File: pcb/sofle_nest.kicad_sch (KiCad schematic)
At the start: 110 parts, among them J1 MJ-4PP-9, J2 Pheonix-1332645, J3 Conn_01x04, J4 FFC2B35-12-G_REVA2, SW1 SW_PUSH, SW10 SW_PUSH, SW11 SW_PUSH, SW12 SW_PUSH, SW13 SW_PUSH, SW14 SW_PUSH, SW15 SW_PUSH, SW16 SW_PUSH, SW17 SW_PUSH, SW18 SW_PUSH, SW19 SW_PUSH, SW2 SW_PUSH, SW20 SW_PUSH, SW21 SW_PUSH, SW22 SW_PUSH, SW23 SW_PUSH, SW24 SW_PUSH, SW25 Rotary_Encoder_Switch-Device, SW26 SW_PUSH, SW27 SW_PUSH, SW28 SW_PUSH, SW29 SW_PUSH, SW3 SW_PUSH, SW30 SW_PUSH, SW4 SW_PUSH, SW5 SW_PUSH, SW6 SW_PUSH, SW7 SW_PUSH, SW8 SW_PUSH, SW9 SW_PUSH, U2 kb2040

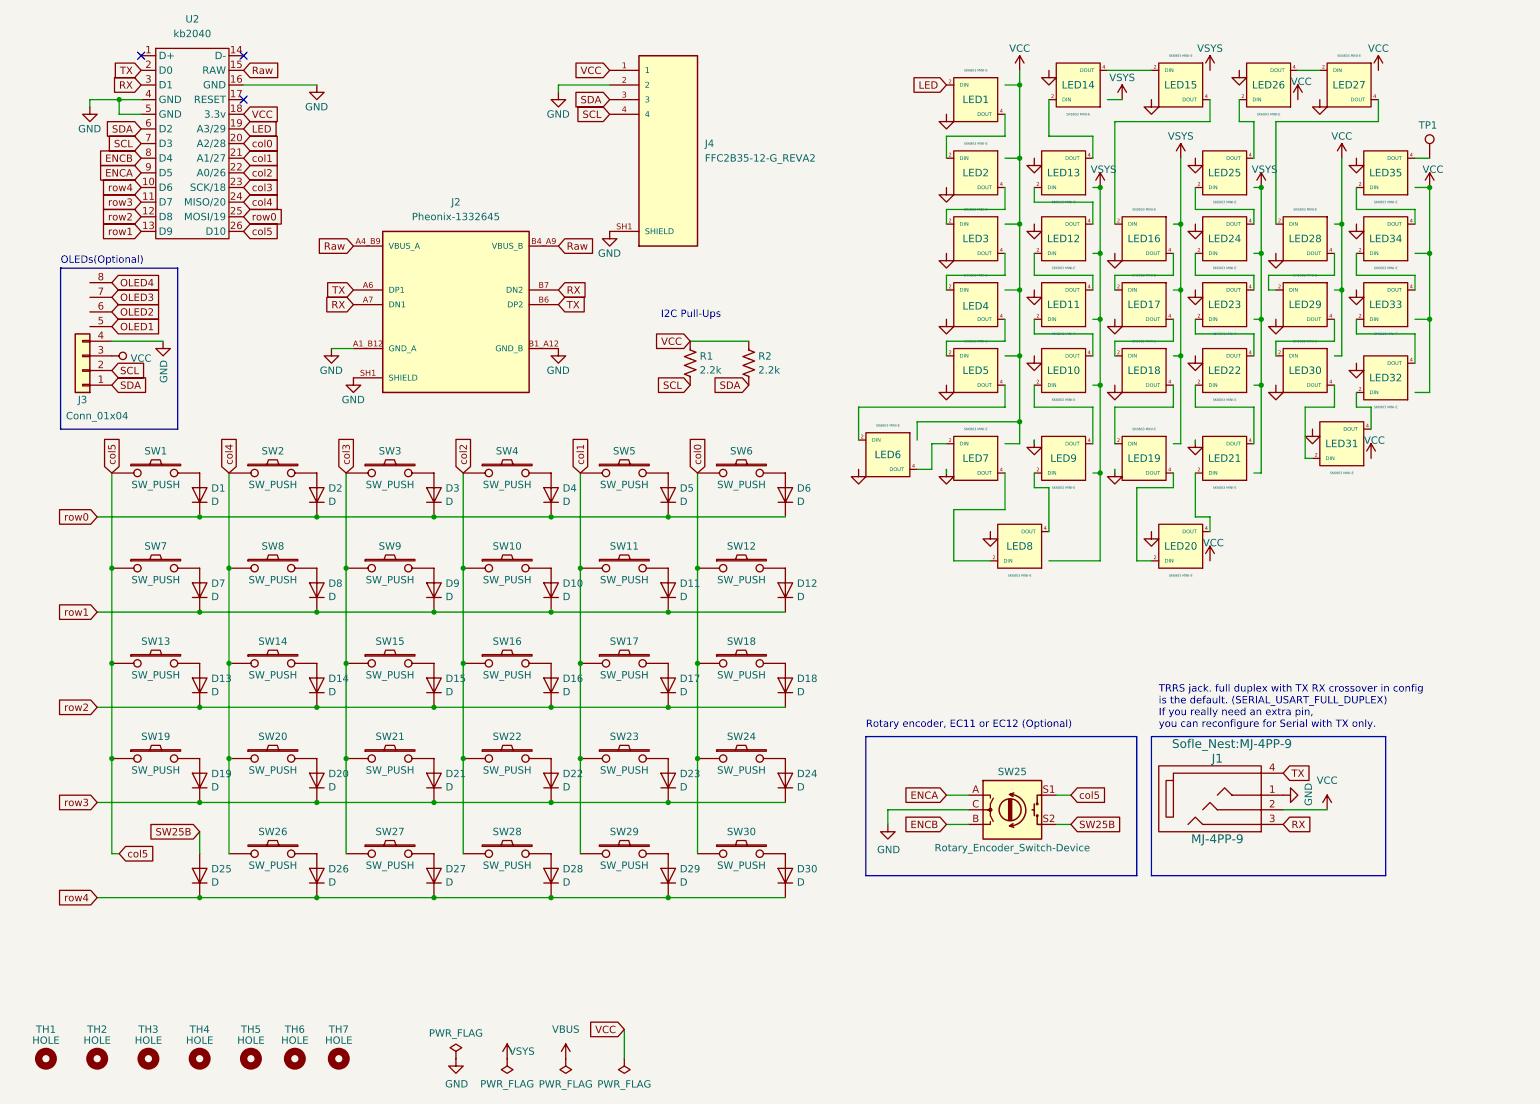
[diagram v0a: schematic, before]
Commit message: Re-route underglow leds to put the top ones in series
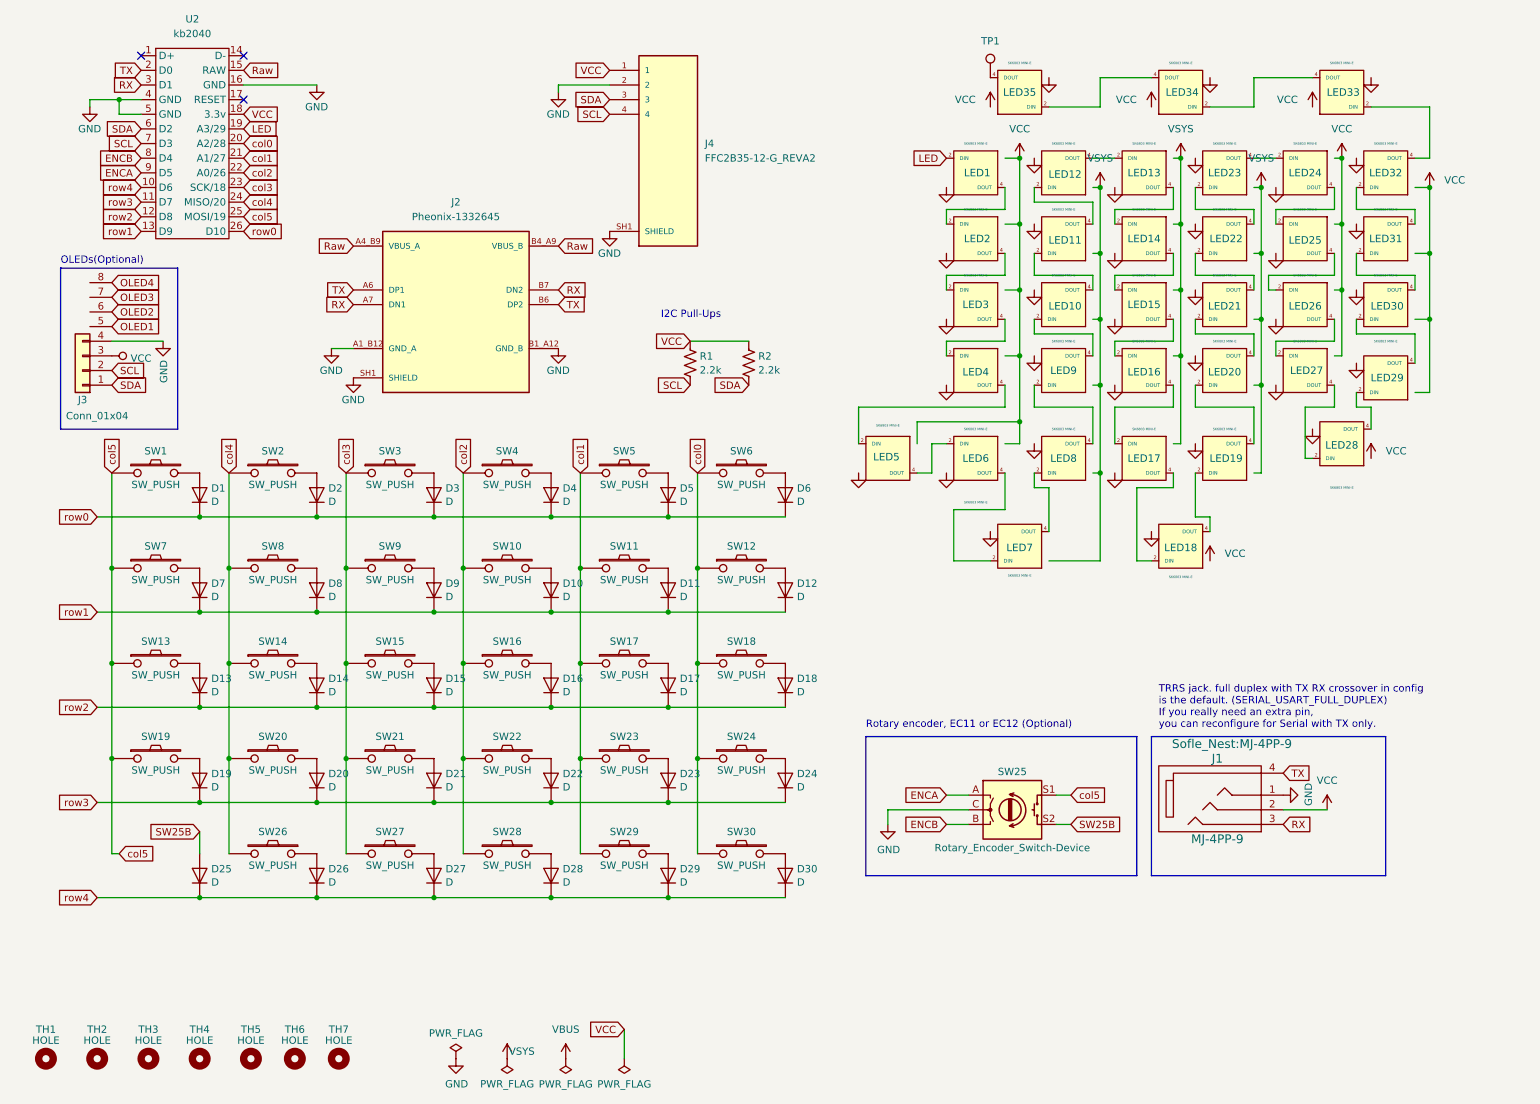
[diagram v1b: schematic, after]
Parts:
- LED1, LED20, LED31, LED8: footprint Sofle_Nest:DropLight_SK6803_MINI-E_v3.5.5 -> Sofle_Nest:SK6803_MINI-E_v3.5.5; symbol Sofle_Nest:DropLight_SK6803MINIE_V2 -> Sofle_Nest:SK6803MINIE_V2
- LED15, LED27: footprint Sofle_Nest:DropLight_SK6803_MINI-E_v3.5.5 -> Sofle_Nest:SK6803_MINI-E_v3.5.5
- LED18, LED28, LED33, LED34, LED35, LED7: footprint Sofle_Nest:SK6803_MINI-E_v3.5.5 -> Sofle_Nest:SK6803_MINI-E_v3.5.5_Underglow; symbol Sofle_Nest:SK6803MINIE_V2 -> Sofle_Nest:SK6803MINIE_V2_Underglow
- LED26: symbol Sofle_Nest:DropLight_SK6803MINIE_V2 -> Sofle_Nest:SK6803MINIE_V2
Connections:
- net col5: now also U2.25 (MOSI/19); no longer U2.26 (D10)
- net row0: now also U2.26 (D10); no longer U2.25 (MOSI/19)
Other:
- moved on the sheet: LED1, LED10, LED11, LED12, LED13, LED14, LED15, LED16, LED17, LED18, LED19, LED2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

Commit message: Update schematic to pass electrical check rules and rewrite LEDs row-wise
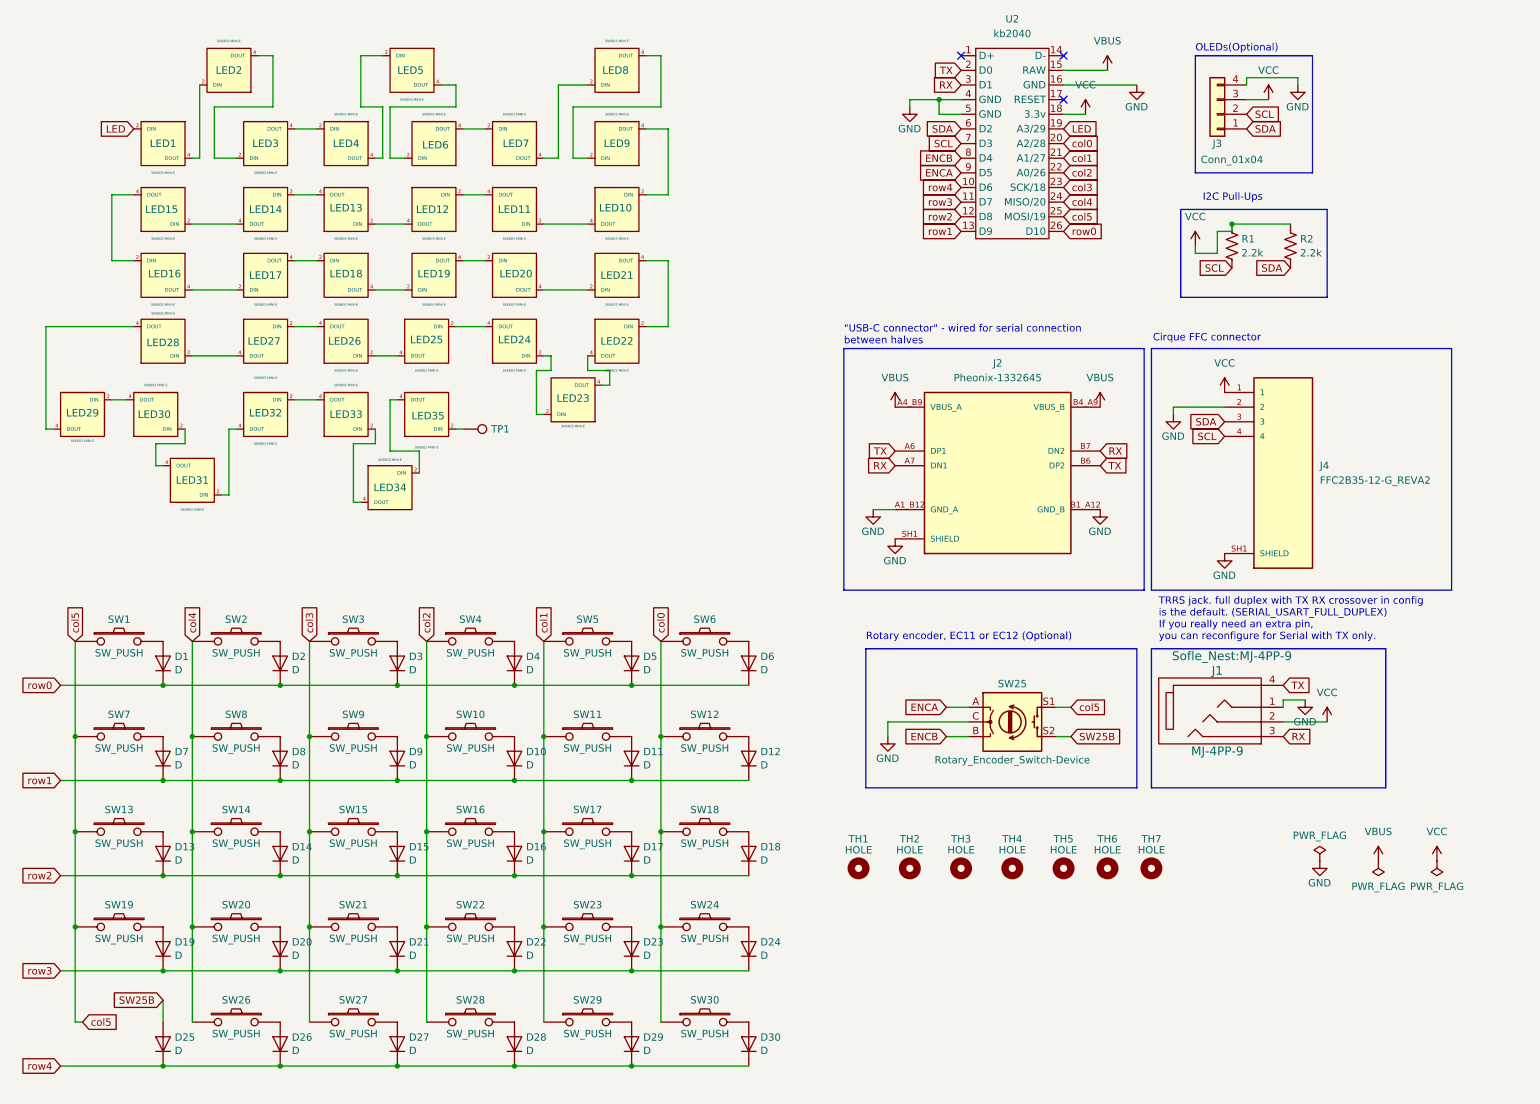
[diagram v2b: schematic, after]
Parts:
- J1: symbol Sofle_Pico:MJ-4PP-9 -> Sofle_Nest:MJ-4PP-9
- LED23: renamed from LED4; footprint Sofle_Nest:SK6803_MINI-E_v3.5.5 -> Sofle_Nest:SK6803_MINI-E_v3.5.5_Underglow; symbol Sofle_Nest:SK6803MINIE_V2 -> Sofle_Nest:SK6803MINIE_V2_Underglow
- LED28: renamed from LED18; footprint Sofle_Nest:SK6803_MINI-E_v3.5.5_Underglow -> Sofle_Nest:SK6803_MINI-E_v3.5.5; symbol Sofle_Nest:SK6803MINIE_V2_Underglow -> Sofle_Nest:SK6803MINIE_V2
- LED29: renamed from LED28; footprint Sofle_Nest:SK6803_MINI-E_v3.5.5_Underglow -> Sofle_Nest:SK6803_MINI-E_v3.5.5; symbol Sofle_Nest:SK6803MINIE_V2_Underglow -> Sofle_Nest:SK6803MINIE_V2
- LED31: renamed from LED17; footprint Sofle_Nest:SK6803_MINI-E_v3.5.5 -> Sofle_Nest:SK6803_MINI-E_v3.5.5_Underglow; symbol Sofle_Nest:SK6803MINIE_V2 -> Sofle_Nest:SK6803MINIE_V2_Underglow
- LED32: renamed from LED7; footprint Sofle_Nest:SK6803_MINI-E_v3.5.5_Underglow -> Sofle_Nest:SK6803_MINI-E_v3.5.5; symbol Sofle_Nest:SK6803MINIE_V2_Underglow -> Sofle_Nest:SK6803MINIE_V2
- LED34: renamed from LED6; footprint Sofle_Nest:SK6803_MINI-E_v3.5.5 -> Sofle_Nest:SK6803_MINI-E_v3.5.5_Underglow; symbol Sofle_Nest:SK6803MINIE_V2 -> Sofle_Nest:SK6803MINIE_V2_Underglow
- SW25: symbol Sofle_Pico:Rotary_Encoder_Switch-Device -> Sofle_Nest:Rotary_Encoder_Switch-Device
- renumbered LED23 to LED1, LED11 to LED10, LED14 to LED11, LED22 to LED12, LED25 to LED13, LED31 to LED14, LED2 to LED15, LED10 to LED16, LED15 to LED17, LED21 to LED18, LED26 to LED19, LED35 to LED2, LED30 to LED20, LED3 to LED21, LED9 to LED22, LED16 to LED24, LED20 to LED25, LED27 to LED26, LED29 to LED27, LED24 to LED3, LED19 to LED30, LED8 to LED33, LED5 to LED35, LED13 to LED4, LED34 to LED5, LED12 to LED6, LED1 to LED7, LED33 to LED8, LED32 to LED9
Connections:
- net Raw is gone; now on net VBUS: J2.A4_B9 (VBUS_A), J2.B4_A9 (VBUS_B), U2.15 (RAW)
- net LED: now also LED1.2 (DIN); no longer LED7.2 (DIN)
- net at LED22.2 (DIN): now also LED21.4 (DOUT); no longer LED33.4 (DOUT)
- net at LED22.4 (DOUT): now also LED23.4 (DOUT); no longer LED16.2 (DIN)
- net at LED14.2 (DIN): now also LED13.4 (DOUT); no longer LED20.4 (DOUT)
- net at LED14.4 (DOUT): now also LED15.2 (DIN); no longer LED9.2 (DIN)
- net at LED30.2 (DIN): now also LED31.4 (DOUT); no longer LED28.4 (DOUT)
- net at LED30.4 (DOUT): now also LED29.2 (DIN); no longer LED25.2 (DIN)
- net at LED21.2 (DIN): now also LED20.4 (DOUT); no longer LED15.4 (DOUT)
- net at LED23.2 (DIN): now also LED24.2 (DIN); no longer LED21.4 (DOUT)
- net at LED20.2 (DIN): now also LED19.4 (DOUT); no longer LED27.4 (DOUT)
- net at LED5.2 (DIN): now also LED4.4 (DOUT); no longer LED8.4 (DOUT)
- net at LED5.4 (DOUT): now also LED6.2 (DIN); no longer LED2.2 (DIN)
- net at LED31.2 (DIN): now also LED32.4 (DOUT); no longer LED24.4 (DOUT)
- net at LED28.2 (DIN): now also LED27.4 (DOUT); no longer LED31.4 (DOUT)
- net at LED4.2 (DIN): now also LED3.4 (DOUT); no longer LED6.4 (DOUT)
- net at LED11.2 (DIN): now also LED10.4 (DOUT); no longer LED4.4 (DOUT)
- net at LED9.4 (DOUT): now also LED10.2 (DIN); no longer LED8.2 (DIN)
- net at LED3.2 (DIN): now also LED2.4 (DOUT); no longer LED1.4 (DOUT)
- net at LED13.2 (DIN): now also LED12.4 (DOUT); no longer LED3.4 (DOUT)
- net at LED27.2 (DIN): now also LED26.4 (DOUT); no longer LED29.4 (DOUT)
- net at LED26.2 (DIN): now also LED25.4 (DOUT); no longer LED19.4 (DOUT)
- net at LED19.2 (DIN): now also LED18.4 (DOUT); no longer LED13.4 (DOUT)
- net at LED18.2 (DIN): now also LED17.4 (DOUT); no longer LED25.4 (DOUT)
- net at LED12.2 (DIN): now also LED11.4 (DOUT); no longer LED18.4 (DOUT)
- net at TP1.1: now also LED35.2 (DIN); no longer LED2.4 (DOUT)
- net at LED16.4 (DOUT): now also LED17.2 (DIN); no longer LED10.2 (DIN)
- net at LED33.2 (DIN): now also LED34.4 (DOUT); no longer LED32.4 (DOUT)
- net at LED7.4 (DOUT): now also LED8.2 (DIN); no longer LED15.2 (DIN)
- net at LED32.2 (DIN): now also LED33.4 (DOUT); no longer LED34.4 (DOUT)
- net OLED1: no longer names the net of J3.5 (Pin_1)
- net OLED2: no longer names the net of J3.6 (Pin_2)
- net OLED3: no longer names the net of J3.7 (Pin_3)
- net OLED4: no longer names the net of J3.8 (Pin_4)
- new net: LED8.4 (DOUT), LED9.2 (DIN)
- new net: LED28.4 (DOUT), LED29.4 (DOUT)
- new net: LED1.4 (DOUT), LED2.2 (DIN)
- new net: LED6.4 (DOUT), LED7.2 (DIN)
- new net: LED15.4 (DOUT), LED16.2 (DIN)
- new net: LED24.4 (DOUT), LED25.2 (DIN)
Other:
- note added: ""USB-C connector" - wired for serial connection between halves"
- note added: "Cirque FFC connector"
- moved on the sheet: D1, D10, D11, D12, D13, D14, D15, D16, D17, D18, D19, D2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

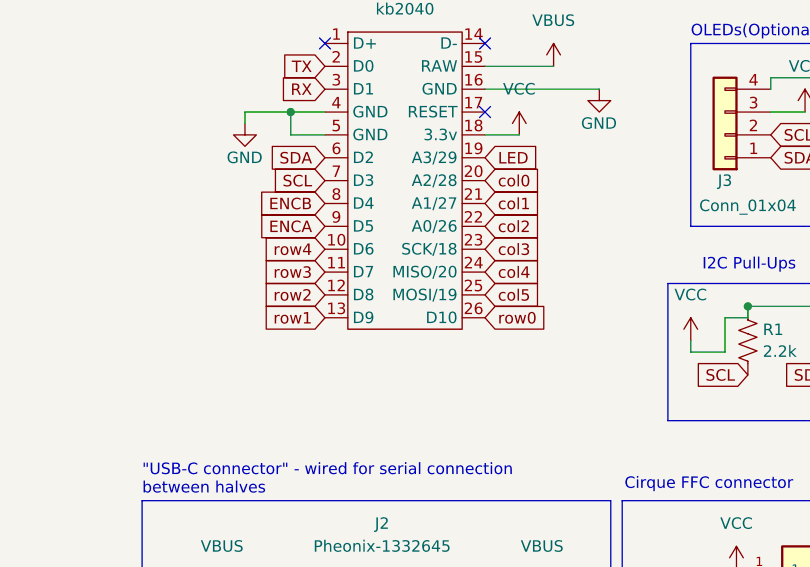
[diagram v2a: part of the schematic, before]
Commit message: Rewire rows and columns
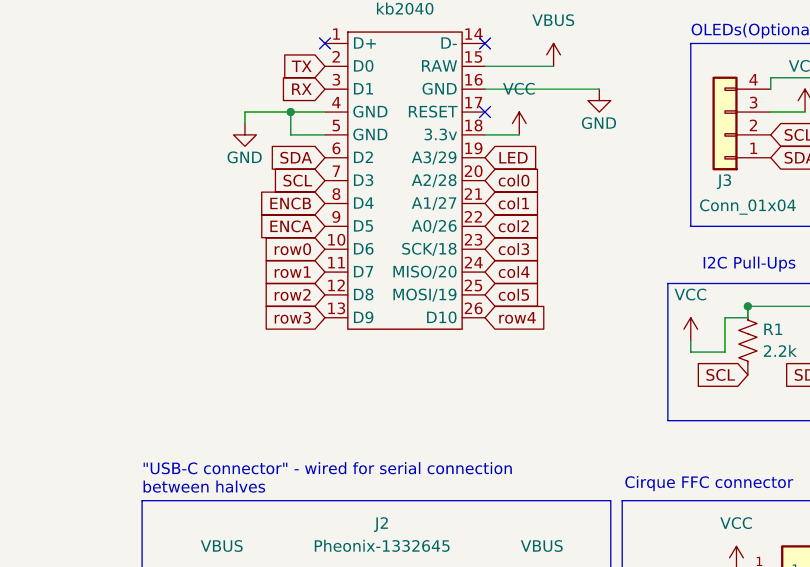
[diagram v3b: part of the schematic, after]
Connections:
- net row0: now also U2.10 (D6); no longer U2.26 (D10)
- net row1: now also U2.11 (D7); no longer U2.13 (D9)
- net row3: now also U2.13 (D9); no longer U2.11 (D7)
- net row4: now also U2.26 (D10); no longer U2.10 (D6)
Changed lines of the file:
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@@
-		)
-	)
-	(global_label "row0"
-		(shape input)
-		(at 195.58 53.34 0)
-		(effects
-			(font
-				(size 1.27 1.27)
-			)
-			(justify left)
-		)
-		(property "Intersheetrefs" "${INTERSHEET_REFS}"
-			(at 195.58 53.34 0)
-			(effects
-				(font
-					(size 1.27 1.27)
-				)
-				(hide yes)
-			)
 		)
 	)
@@
 		)
 	)
+	(global_label "row3"
+		(shape input)
+		(at 177.8 53.34 180)
+		(effects
+			(font
+				(size 1.27 1.27)
+			)
+			(justify right)
+		)
+		(property "Intersheetrefs" "${INTERSHEET_REFS}"
+			(at 177.8 53.34 0)
+			(effects
+				(font
+					(size 1.27 1.27)
+				)
+				(hide yes)
+			)
+		)
+	)
 	(global_label "LED"
 		(shape input)
@@
 		)
 	)
+	(global_label "row4"
+		(shape input)
+		(at 195.58 53.34 0)
+		(effects
+			(font
+				(size 1.27 1.27)
+			)
+			(justify left)
+		)
+		(property "Intersheetrefs" "${INTERSHEET_REFS}"
+			(at 195.58 53.34 0)
+			(effects
+				(font
+					(size 1.27 1.27)
+				)
+				(hide yes)
+			)
+		)
+	)
+	(global_label "row1"
+		(shape input)
+		(at 177.8 48.26 180)
+		(effects
+			(font
+				(size 1.27 1.27)
+			)
+			(justify right)
+		)
+		(property "Intersheetrefs" "${INTERSHEET_REFS}"
+			(at 177.8 48.26 0)
+			(effects
+				(font
+					(size 1.27 1.27)
+				)
+				(hide yes)
+			)
+		)
+	)
 	(global_label "TX"
 		(shape input)
@@
 		)
 	)
-	(global_label "row4"
+	(global_label "col3"
+		(shape input)
+		(at 64.77 124.46 90)
+		(effects
+			(font
+				(size 1.27 1.27)
+			)
+			(justify left)
+		)
+		(property "Intersheetrefs" "${INTERSHEET_REFS}"
+			(at 64.77 124.46 0)
+			(effects
+				(font
+					(size 1.27 1.27)
+				)
+				(hide yes)
+			)
+		)
+	)
+	(global_label "SW25B"
+		(shape input)
+		(at 196.85 140.97 0)
+		(effects
+			(font
+				(size 1.27 1.27)
+			)
+			(justify left)
+		)
+		(property "Intersheetrefs" "${INTERSHEET_REFS}"
+			(at 196.85 140.97 0)
+			(effects
+				(font
+					(size 1.27 1.27)
+				)
+				(hide yes)
+			)
+		)
+	)
+	(global_label "LED"
+		(shape input)
+		(at 195.58 35.56 0)
+		(effects
+			(font
+				(size 1.27 1.27)
+			)
+			(justify left)
+		)
+		(property "Intersheetrefs" "${INTERSHEET_REFS}"
+			(at 195.58 35.56 0)
+			(effects
+				(font
+					(size 1.27 1.27)
+				)
+				(hide yes)
+			)
+		)
+	)
+	(global_label "row0"
 		(shape input)
 		(at 177.8 45.72 180)
@@
 		)
 	)
-	(global_label "col3"
-		(shape input)
-		(at 64.77 124.46 90)
-		(effects
-			(font
-				(size 1.27 1.27)
-			)
-			(justify left)
-		)
-		(property "Intersheetrefs" "${INTERSHEET_REFS}"
-			(at 64.77 124.46 0)
-			(effects
-				(font
-					(size 1.27 1.27)
-				)
-				(hide yes)
-			)
-		)
-	)
-	(global_label "SW25B"
-		(shape input)
-		(at 196.85 140.97 0)
-		(effects
-			(font
-				(size 1.27 1.27)
-			)
-			(justify left)
-		)
-		(property "Intersheetrefs" "${INTERSHEET_REFS}"
-			(at 196.85 140.97 0)
-			(effects
-				(font
-					(size 1.27 1.27)
-				)
-				(hide yes)
-			)
-		)
-	)
-	(global_label "LED"
-		(shape input)
-		(at 195.58 35.56 0)
-		(effects
-			(font
-				(size 1.27 1.27)
-			)
-			(justify left)
-		)
-		(property "Intersheetrefs" "${INTERSHEET_REFS}"
-			(at 195.58 35.56 0)
-			(effects
-				(font
-					(size 1.27 1.27)
-				)
-				(hide yes)
-			)
-		)
-	)
 	(global_label "row1"
 		(shape input)
@@
 		(property "Intersheetrefs" "${INTERSHEET_REFS}"
 			(at 21.59 148.59 0)
-			(effects
-				(font
-					(size 1.27 1.27)
-				)
-				(hide yes)
-			)
-		)
-	)
-	(global_label "row1"
-		(shape input)
-		(at 177.8 53.34 180)
-		(effects
-			(font
-				(size 1.27 1.27)
-			)
-			(justify right)
-		)
-		(property "Intersheetrefs" "${INTERSHEET_REFS}"
-			(at 177.8 53.34 0)
 			(effects
 				(font
@@
 			(effects
 				(font
-					(size 1.27 1.27)
-				)
-				(hide yes)
-			)
-		)
-	)
-	(global_label "row3"
-		(shape input)
-		(at 177.8 48.26 180)
-		(effects
-			(font
-				(size 1.27 1.27)
-			)
-			(justify right)
-		)
-		(property "Intersheetrefs" "${INTERSHEET_REFS}"
-			(at 177.8 48.26 0)
-			(effects
-				(font
